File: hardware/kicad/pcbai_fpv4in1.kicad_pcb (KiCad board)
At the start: 6 copper layers, 90 x 75 mm, 364 parts, among them J1 BATT_PAD, J10 VSUP_5V_TBD, J11 TLV76733DRVR, J12 SM08B-SRSS-TB, J13 USBLC6-2SC6, J14 USBLC6-2SC6, J15 USBLC6-2SC6, J16 AT32F421K8T7, J17 DRV8300DRGER, J18 INA186A3IDCKR, J19 INA186A3IDCKR, J2 TPS54560DDAR, J20 INA186A3IDCKR, J21 AT32F421K8T7, J22 DRV8300DRGER, J23 INA186A3IDCKR, J24 INA186A3IDCKR, J25 INA186A3IDCKR, J26 AT32F421K8T7, J27 DRV8300DRGER, J28 INA186A3IDCKR, J29 INA186A3IDCKR, J3 TPS54560DDAR, J30 INA186A3IDCKR, J31 AT32F421K8T7, J32 DRV8300DRGER, J33 INA186A3IDCKR, J34 INA186A3IDCKR, J35 INA186A3IDCKR, J4 TPS54560DDAR, J5 AOZ1284PI, J6 AOZ1284PI, J7 TPS259251DRCR, J8 TPS259251DRCR, J9 TPS259251DRCR, Q1 AON6260, Q10 AOTL66912, Q11 AOTL66912, Q12 AOTL66912, Q13 AOTL66912, Q14 AOTL66912, Q15 AOTL66912, Q16 AOTL66912, Q17 AOTL66912, Q18 AOTL66912, Q19 AOTL66912, Q2 AON6260, Q20 AOTL66912, Q21 AOTL66912, Q22 AOTL66912, Q23 AOTL66912, Q24 AOTL66912, Q25 AOTL66912, Q26 AOTL66912, Q27 AOTL66912, Q28 AOTL66912, Q3 AON6260, Q4 AON6260, Q5 AOTL66912, Q6 AOTL66912, Q7 AOTL66912, Q8 AOTL66912, Q9 AOTL66912

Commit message: Phase 5b: DSN tooling + diagnostic (autoroute deferred to post-4b-redo3)
Autoroute did not converge against the Phase 4b-redo2 placement (90×75 board,
F.Cu util ~62%). Three Freerouting runs empirically confirmed an F.Cu
signal-density bottleneck:

  Run 1: 2-layer DSN, no planes — 68.7% completion (78 unrouted / 249 nets)
  Run 2: 2-layer DSN, planes after (via) [wrong order] — killed at 25 min
  Run 3: 4-layer DSN with pseudo In1.Cu + In2.Cu planes — killed at 14 min;
         1069+ "MazeSearchAlgo: no accessible expansion doors" failures

Per master adjudication 2026-05-22: trigger Phase 4b-redo3
(grow 90×75 → 100×85 + signal-density gate + buck-column relief).

What's committed in this PR:

1. setup_board.py — 3 side-fixes for ExportSpecctraDSN silent-fail modes:
   (a) Edge.Cuts: 4 gr_lines → gr_rect (closed polygon required)
   (b) Mount-hole footprints: emit complete KiCad9 format with uuid/descr/
       Reference/Value (was minimal stub causing silent export failure)
   (c) Skip 6-layer upgrade — kept 2-layer for autoroute (planes added via
       DSN injection, expanded back to 6-layer in Phase 5c after route)

2. scripts/export_dsn.py — NEW. pcbnew Specctra DSN export wrapper.

3. scripts/dsn_strip_planes.py — NEW. Playbook trap T1 plane-stripper;
   idempotent (pass-through for current 2-layer state).

4. scripts/dsn_inject_planes.py — NEW. Adds 4-layer pseudo-structure to DSN:
   In1.Cu + In2.Cu signal-typed layers + GND/+VMOTOR/+3V3 planes + padstack
   through-hole expansion. Works around master's playbook T1 incomplete recipe.

5. PHASE5B_DIAGNOSTIC.md — concise (65 lines) per master directive:
   what was tried, why each failed, what's deferred.

Findings worth surfacing as cross-master lessons:

  - Playbook §Routing T1 ("omit planes from DSN") is incomplete recipe;
    works only for simple boards. Dense placements need planes for
    plane-served exclusion from autoroute.
  - ExportSpecctraDSN has 3 silent-fail modes documented above.
  - Plane or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
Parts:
- removed ? (x4): , MountingHole:MountingHole_3.2mm_M3
- added H1: MountingHole, MountingHole:MountingHole_3.2mm_M3, F.Cu at (5.00, 5.00)
- added H2: MountingHole, MountingHole:MountingHole_3.2mm_M3, F.Cu at (85.0, 5.00)
- added H3: MountingHole, MountingHole:MountingHole_3.2mm_M3, F.Cu at (5.00, 70.0)
- added H4: MountingHole, MountingHole:MountingHole_3.2mm_M3, F.Cu at (85.0, 70.0)
- moved J21 94.6 mm to (82.0, 8.00), turned to 90 degrees
- moved J26 94.6 mm to (8.00, 8.00), turned to 0 degrees
- moved J22 75.0 mm to (75.0, 15.0)
- moved C1 70.0 mm to (80.0, 67.0)
- moved C2 70.0 mm to (10.0, 67.0)
- moved Q17 67.7 mm to (5.00, 28.0)
- moved J29 63.3 mm to (71.0, 19.0)
- moved Q10 62.5 mm to (5.00, 41.0)
- moved R68 61.3 mm to (17.8, 53.0)
- moved C27 60.6 mm to (68.0, 17.8)
- moved C38 60.2 mm to (70.8, 19.2)
- moved R73 60.2 mm to (16.2, 44.0)
- moved J27 60.0 mm to (15.0, 60.0)
- moved R44 59.4 mm to (17.8, 50.2)
- moved C97 59.0 mm to (69.4, 50.2)
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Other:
- copper layers 6 -> 2
- board text removed: "+3V3"
- board text removed: "+5V"
- board text removed: "+9V"
- board text removed: "A"
- board text removed: "AI"
- board text removed: "B"
- board text removed: "BAT+"
- board text removed: "BEC"
- board text removed: "C"
- board text removed: "CH1"
- board text removed: "CH2"
- board text removed: "CH3"
- board text removed: "CH4"
- board text removed: "CURR"
- board text removed: "FC"
- board text removed: "FC CONNECTOR"
- board text removed: "GND"
- board text removed: "M1"
- board text removed: "M2"
- board text removed: "M3"
- board text removed: "M4"
- board text removed: "NTC ICL"
- board text removed: "PHASE3B-MOTOR-RELIEF-BEGIN"
- board text removed: "PHASE3B-MOTOR-RELIEF-END"
- board text removed: "PHASE3B-SILK-BEGIN"
- board text removed: "PHASE3B-SILK-END"
- board text removed: "PWR"
- board text removed: "Pi5"
- board text removed: "REV!"
- board text removed: "Rev A"
- board text removed: "SWCLK"
- board text removed: "SWDIO"
- board text removed: "THERMAL PADS UP TO HEATSINK"
- board text removed: "TLM"
- board text removed: "TP"
- board text removed: "VBAT"
- board text removed: "VTX1"
- board text removed: "VTX2"
- board text removed: "[MFR-MARK]"
- board text removed: "^"
- board text removed: "pcb.ai FPV4in1 v0"

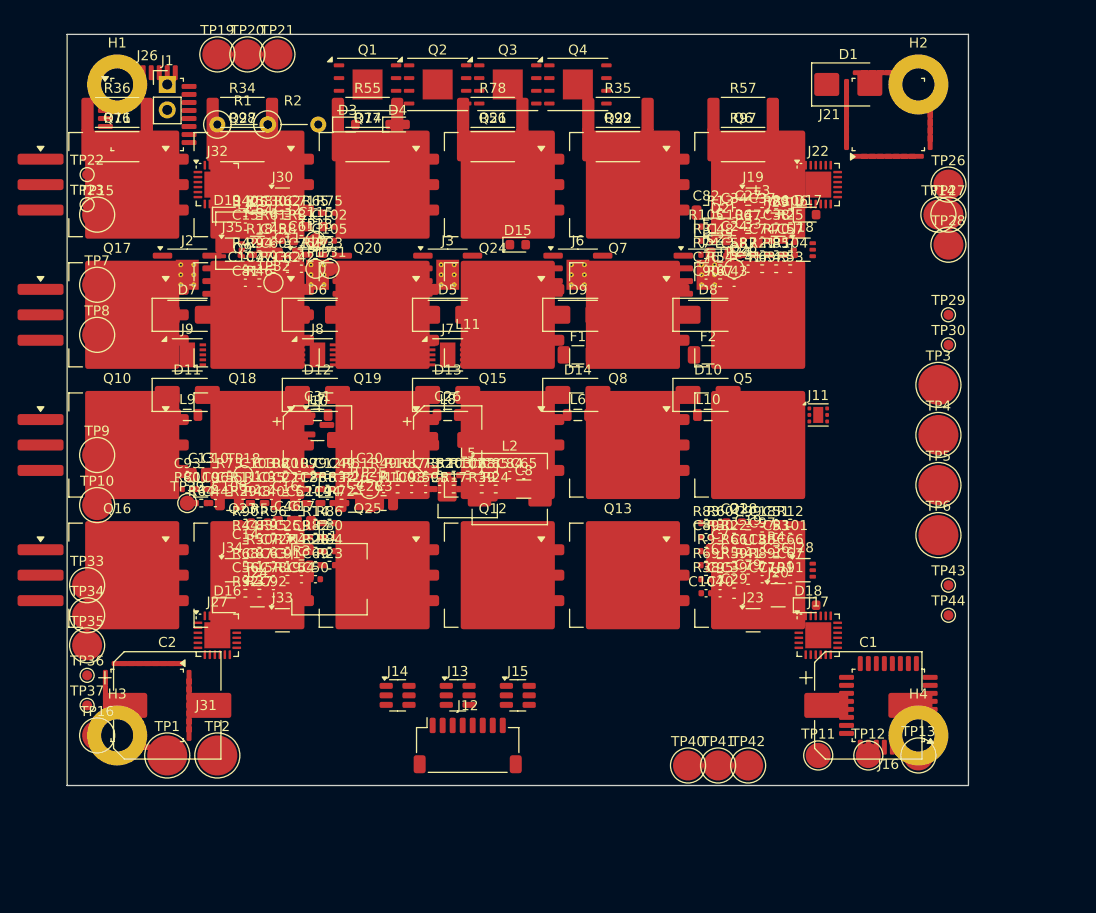
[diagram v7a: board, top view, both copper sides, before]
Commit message: Phase 4b-redo3: grow 90×75 → 100×85 + D/S signal-density gate + In3.Cu signal-promotion
Per master adjudication 2026-05-22 (Phase 5b autoroute failure analysis).

Sanity check confirmed master diagnosis: D/S on 90×75 baseline = 2.06 (way
over 1.0 FAIL threshold) — matches Freerouting Pass #1 = 68.7% empirically.

D/S math after grow + In3.Cu signal-promotion:
  90×75 / 2 signal: D/S = 2.06 (FAIL)
  100×85 / 2 signal: D/S = 1.87 (FAIL — bigger board alone doesn't fix it)
  100×85 / 3 signal (In3.Cu promoted): D/S = 0.83 PASS (15% margin)

Master labeled In3.Cu promotion "secondary non-gating"; D/S math made it
mandatory. In3.Cu signal-promotion is safe — no high-speed differential pairs
or critical impedance constraints in our schematic.

Geometry changes:
  Board: 90×75 → 100×85 (+25.9% area)
  Mount pattern: 80×65 → 90×75 custom (corners (5,5)/(95,5)/(5,80)/(95,80))
  CH2/CH3/CH4 MCUs shifted +10 mm to corners of new outline
  BEC buck strip: y=24..40 → y=29..45 (+5 mm relief)
  BEC col pitch: 13 → 15 mm (+2 mm per col, 60 mm total span)
  BEC passive band: y=44..56 → y=51..63 (+3.5 mm relief)
  BEC passive grid: 25×6@1.4 → 30×6@1.5 (wider + looser)
  FC connector: (40, 71) → (50, 81) re-centered
  All BEC solder pads: distributed on edges with ≥ 2 mm clearance

Phase 4c thermal STAYS VALID — heatsink (80×55 Al6061) unchanged, MOSFET
positions on B.Cu unchanged, model is heatsink-centric.

Carry-forward verified:
  Per-MCU rotation: CH1=0°, CH2=90°, CH3=270°, CH4=180° preserved
  FET-to-channel 3×2 sub-grids preserved
  24 MOSFET physical (x,y) unchanged
  Heatsink valid; Phase 4c verdict (T_J 79.8°C @ Env 2) preserved
  364 footprints; 0 overlaps; 124 silkscreen labels reapplied

R17 fixes per master's pre-emptive flag 2026-05-22:
  dsn_inject_planes.py now parses board outline from DSN (no hardcoded
  90×75 / 100×85). Same for VMOTOR/V3V3 zones. Adds --3signal mode for
  In3.Cu signal-routing. No future loose threads when geometry shifts.

NEW: signal_density_che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
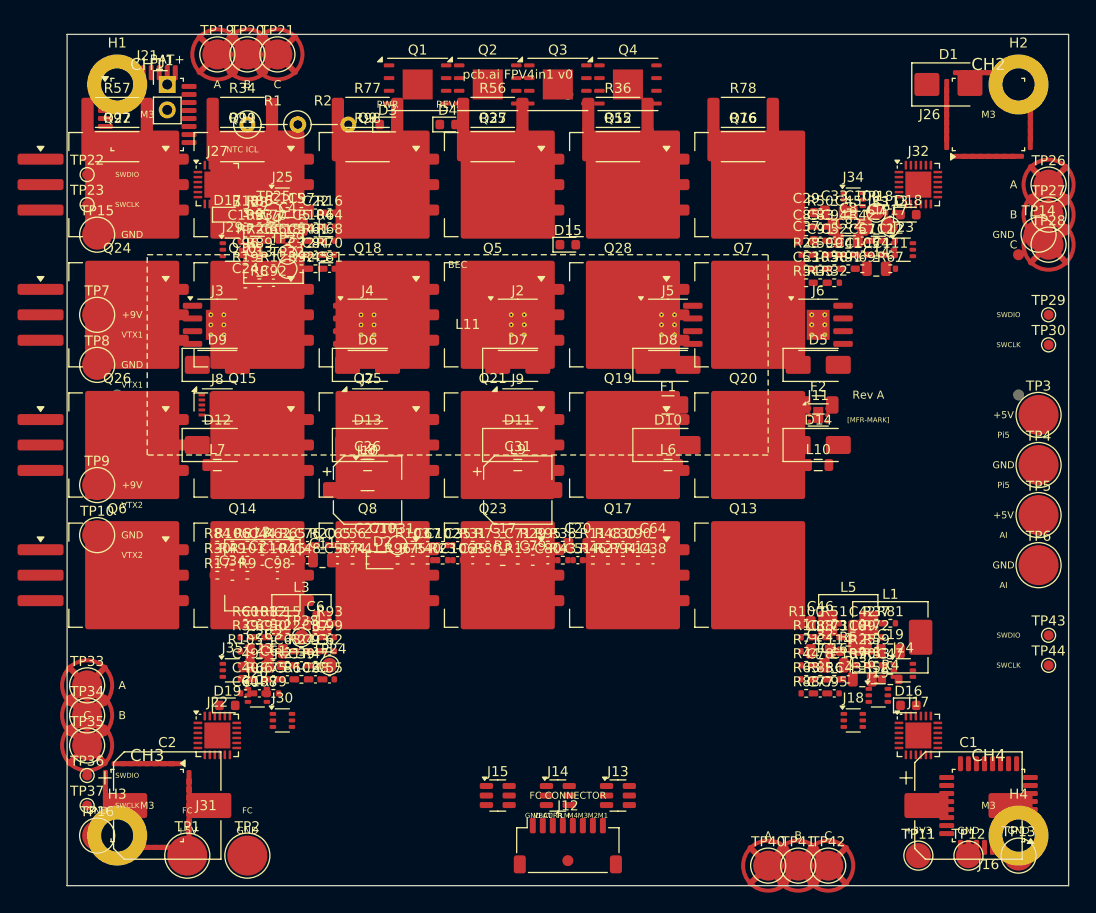
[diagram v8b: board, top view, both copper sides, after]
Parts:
- moved J26 84.0 mm to (92.0, 8.00), turned to 90 degrees
- moved J22 81.4 mm to (15.0, 70.0)
- moved C47 74.4 mm to (82.2, 63.0)
- moved J21 74.0 mm to (8.00, 8.00), turned to 0 degrees
- moved Q16 73.7 mm to (67.5, 15.0)
- moved Q6 73.7 mm to (5.00, 54.0)
- moved J34 72.2 mm to (78.5, 16.5)
- moved C107 72.1 mm to (78.0, 63.0)
- moved J33 71.4 mm to (81.0, 19.0)
- moved R81 70.9 mm to (82.2, 58.8)
- moved J32 70.0 mm to (85.0, 15.0)
- moved C100 69.5 mm to (79.4, 17.8)
- moved C14 69.0 mm to (80.8, 23.4)
- moved D16 68.7 mm to (84.0, 67.0)
- moved TP18 68.4 mm to (80.8, 17.8)
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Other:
- board size 90 x 75 mm -> 100 x 85 mm
- board text added: "+3V3"
- board text added: "+5V"
- board text added: "+9V"
- board text added: "A"
- board text added: "AI"
- board text added: "B"
- board text added: "BAT+"
- board text added: "BEC"
- board text added: "C"
- board text added: "CH1"
- board text added: "CH2"
- board text added: "CH3"
- board text added: "CH4"
- board text added: "CURR"
- board text added: "FC"
- board text added: "FC CONNECTOR"
- board text added: "GND"
- board text added: "M1"
- board text added: "M2"
- board text added: "M3"
- board text added: "M4"
- board text added: "NTC ICL"
- board text added: "PHASE3B-MOTOR-RELIEF-BEGIN"
- board text added: "PHASE3B-MOTOR-RELIEF-END"
- board text added: "PHASE3B-SILK-BEGIN"
- board text added: "PHASE3B-SILK-END"
- board text added: "PWR"
- board text added: "Pi5"
- board text added: "REV!"
- board text added: "Rev A"
- board text added: "SWCLK"
- board text added: "SWDIO"
- board text added: "THERMAL PADS UP TO HEATSINK"
- board text added: "TLM"
- board text added: "TP"
- board text added: "VBAT"
- board text added: "VTX1"
- board text added: "VTX2"
- board text added: "[MFR-MARK]"
- board text added: "^"
- board text added: "pcb.ai FPV4in1 v0"
